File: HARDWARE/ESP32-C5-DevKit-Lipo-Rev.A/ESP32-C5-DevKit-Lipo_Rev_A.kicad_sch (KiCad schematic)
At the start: 80 parts, among them T1 BC817-40(SOT23), T2 BC817-40(SOT23), U1 TP4054-42-SOT25-R, U2 CH340X(MSOP-10), U3 ESP32-C5-WROOM-1-N8R4

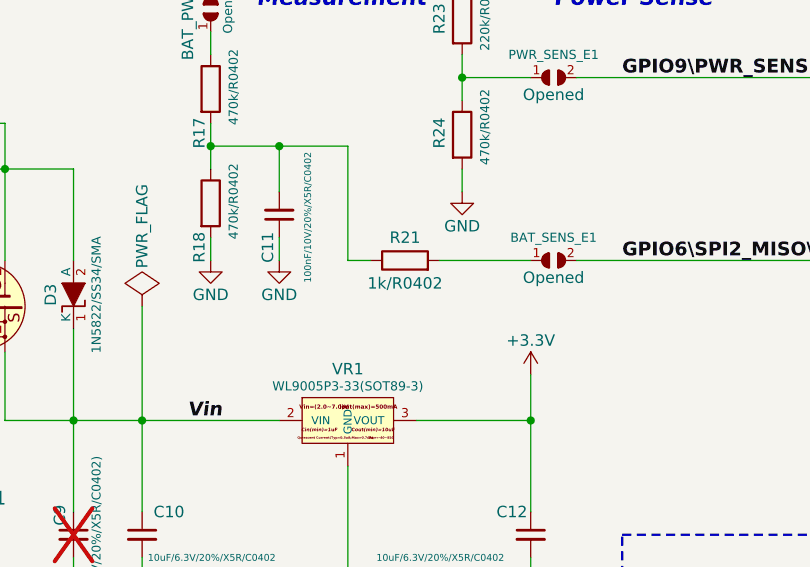
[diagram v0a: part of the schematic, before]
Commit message: Update
Improved battery measurement circuit before board release
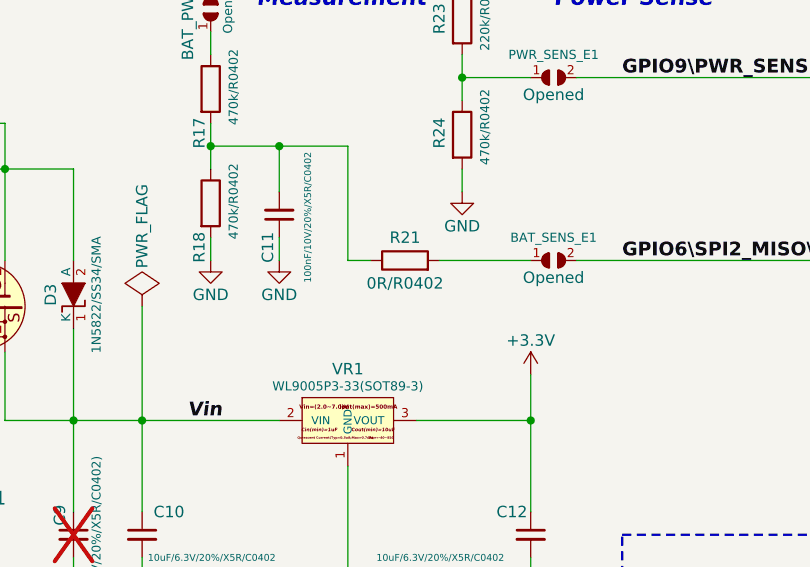
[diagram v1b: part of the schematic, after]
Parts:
- R21: value 1k/R0402 -> 0R/R0402
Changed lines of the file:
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@@
       (effects (font (size 1.27 1.27)))
     )
-    (property "Value" "1k/R0402" (at 146.05 342.9 0)
+    (property "Value" "0R/R0402" (at 146.05 342.9 0)
       (effects (font (size 1.27 1.27)))
     )
